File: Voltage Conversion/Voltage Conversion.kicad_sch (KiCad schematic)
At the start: 27 parts, among them J1 Screw_Terminal_01x01, J10 Screw_Terminal_01x01, J11 Screw_Terminal_01x01, J12 Screw_Terminal_01x01, J2 Screw_Terminal_01x01, J3 Screw_Terminal_01x01, J4 Screw_Terminal_01x01, J9 Screw_Terminal_01x01, U2 LM2596S-ADJ, U3 TPS5431DDA

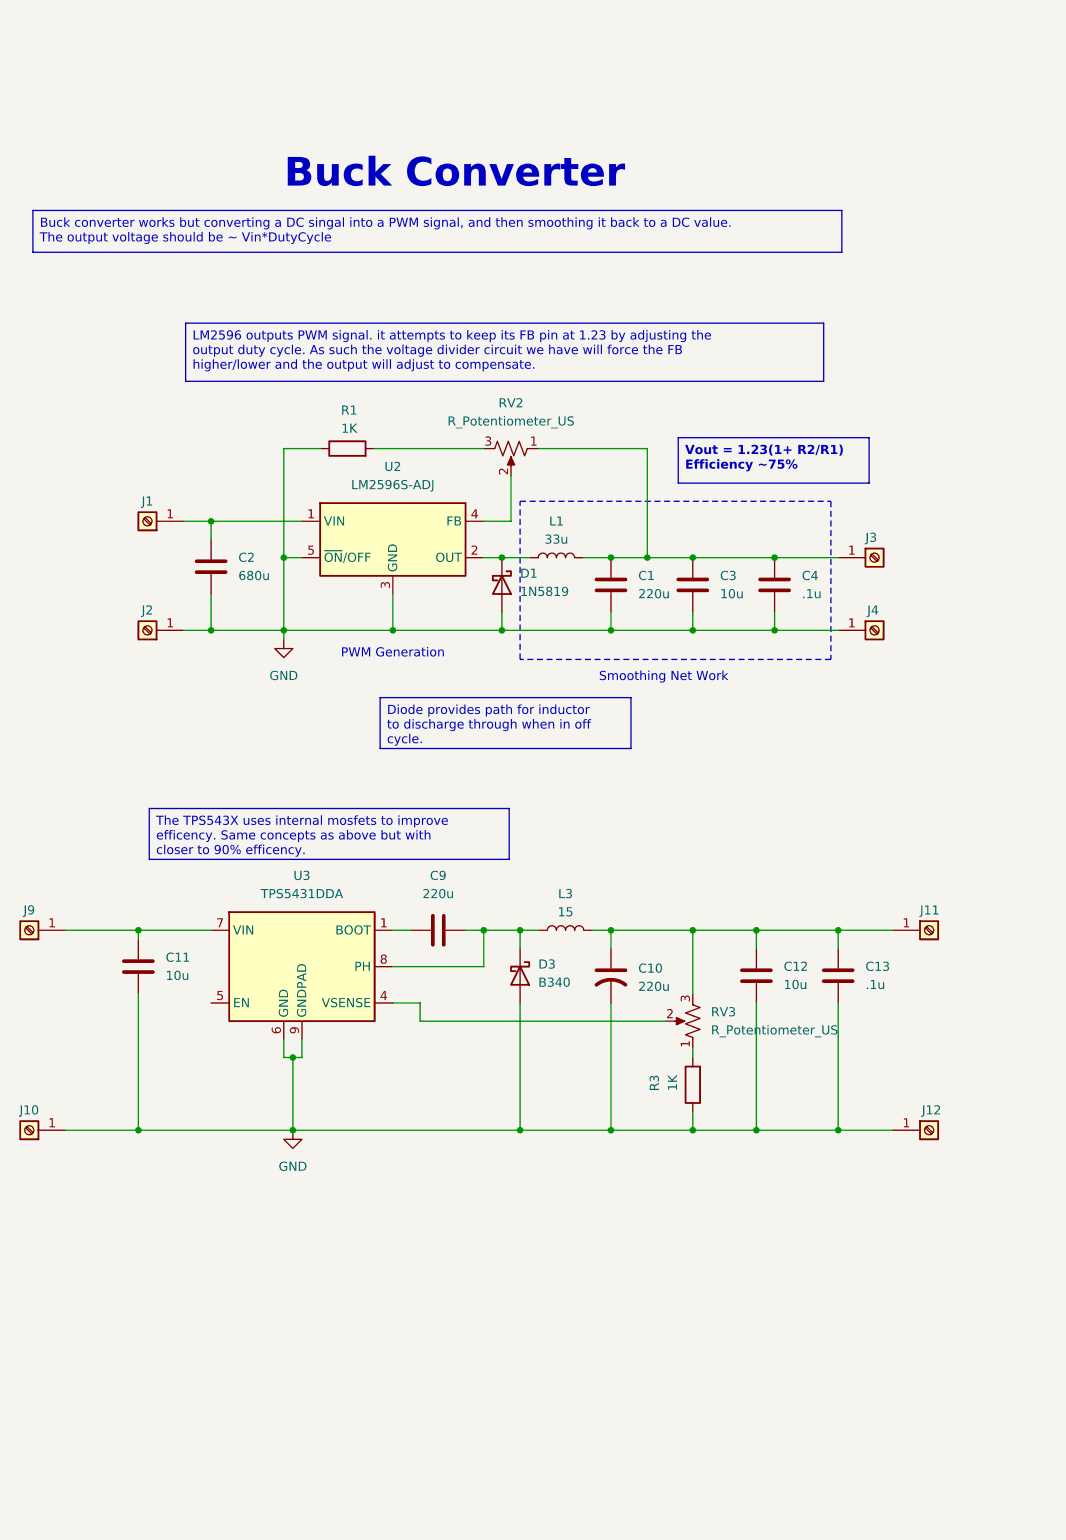
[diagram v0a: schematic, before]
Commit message: Adjustments to ATmega32, README files, Added SEPIC converter to voltage converters, General progress on other designs
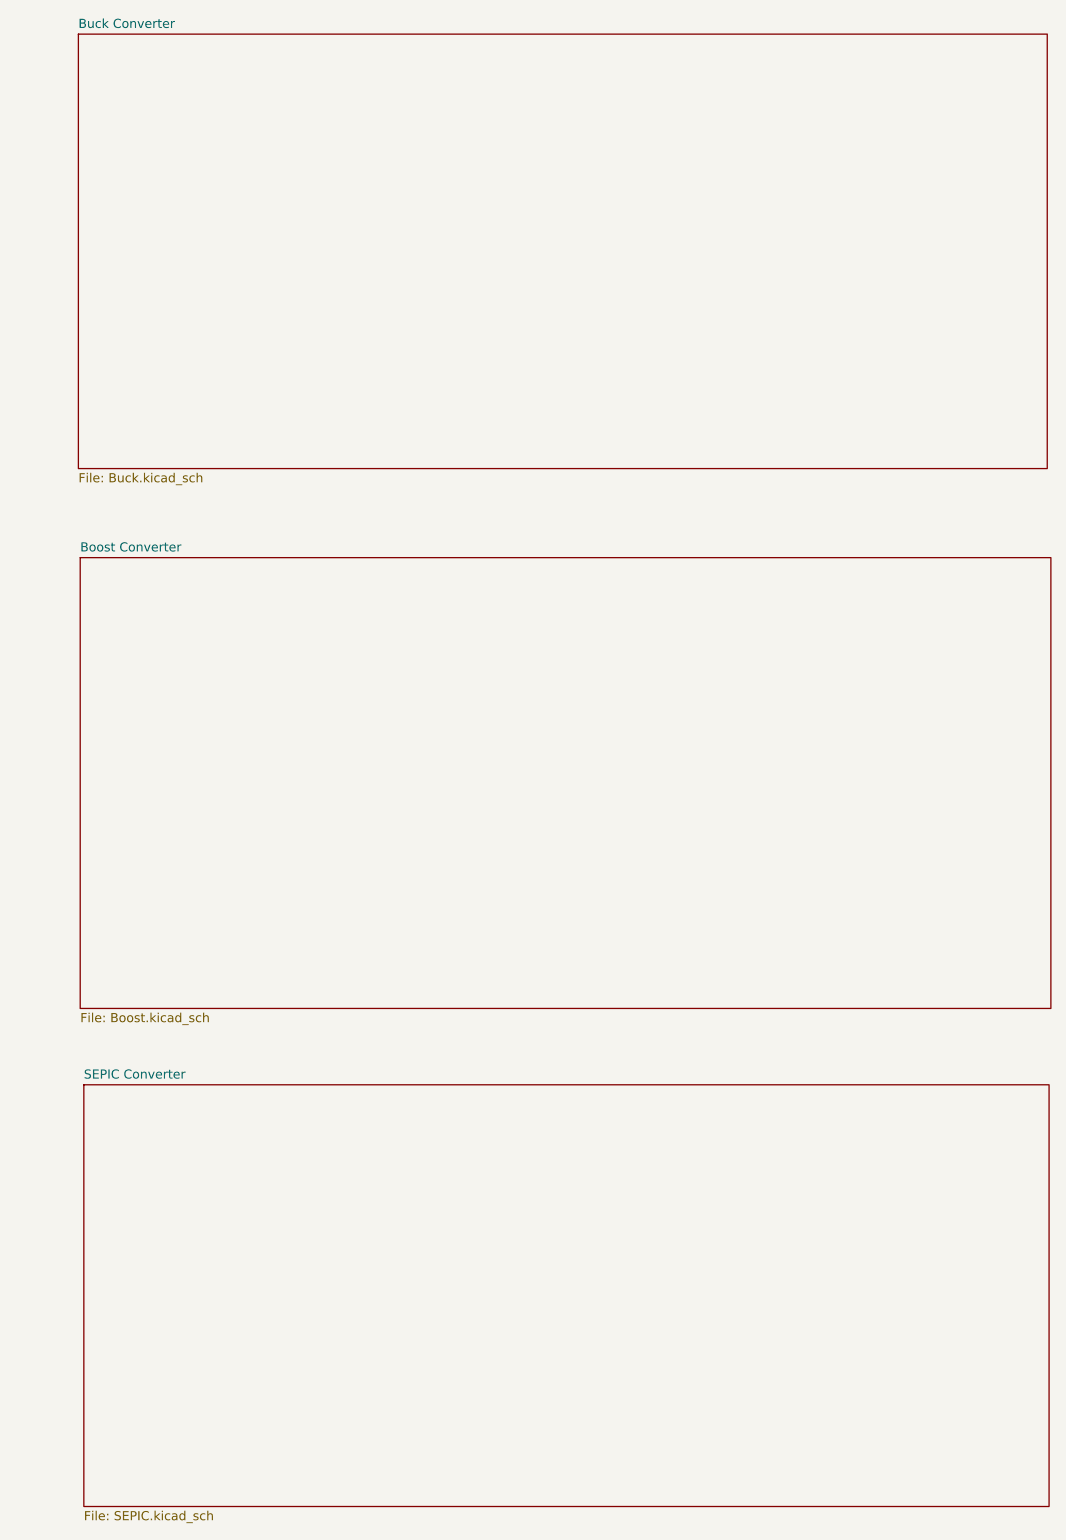
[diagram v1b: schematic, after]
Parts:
- removed C1, C9: 220u, symbol Device:C
- removed C10: 220u, symbol Device:C_US
- removed C11, C12, C3: 10u, symbol Device:C
- removed C13, C4: .1u, symbol Device:C
- removed C2: 680u, symbol Device:C
- removed D1: 1N5819, Diode_THT:D_DO-41_SOD81_P10.16mm_Horizontal, symbol Diode:1N5819
- removed D3: B340, Diode_SMD:D_SMC, symbol Diode:B340
- removed J1, J10, J11, J12, J2, J3, J4, J9: Screw_Terminal_01x01, symbol Connector:Screw_Terminal_01x01
- removed L1: 33u, symbol Device:L
- removed L3: 15, symbol Device:L
- removed R1, R3: 1K, symbol Device:R
- removed RV2, RV3: R_Potentiometer_US, symbol Device:R_Potentiometer_US
- removed U2: LM2596S-ADJ, Package_TO_SOT_SMD:TO-263-5_TabPin3, symbol Regulator_Switching:LM2596S-ADJ
- removed U3: TPS5431DDA, Package_SO:TI_SO-PowerPAD-8_ThermalVias, symbol Regulator_Switching:TPS5431DDA
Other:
- added sheet Boost Converter (Boost.kicad_sch)
- added sheet Buck Converter (Buck.kicad_sch)
- added sheet SEPIC Converter (SEPIC.kicad_sch)
- note removed: "Buck Converter"
- note removed: "PWM Generation"
- note removed: "Smoothing Net Work"
